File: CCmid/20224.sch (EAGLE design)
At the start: 17 parts, among them J3 9296006, K1 PC357NJ0000F, U1 AL8862

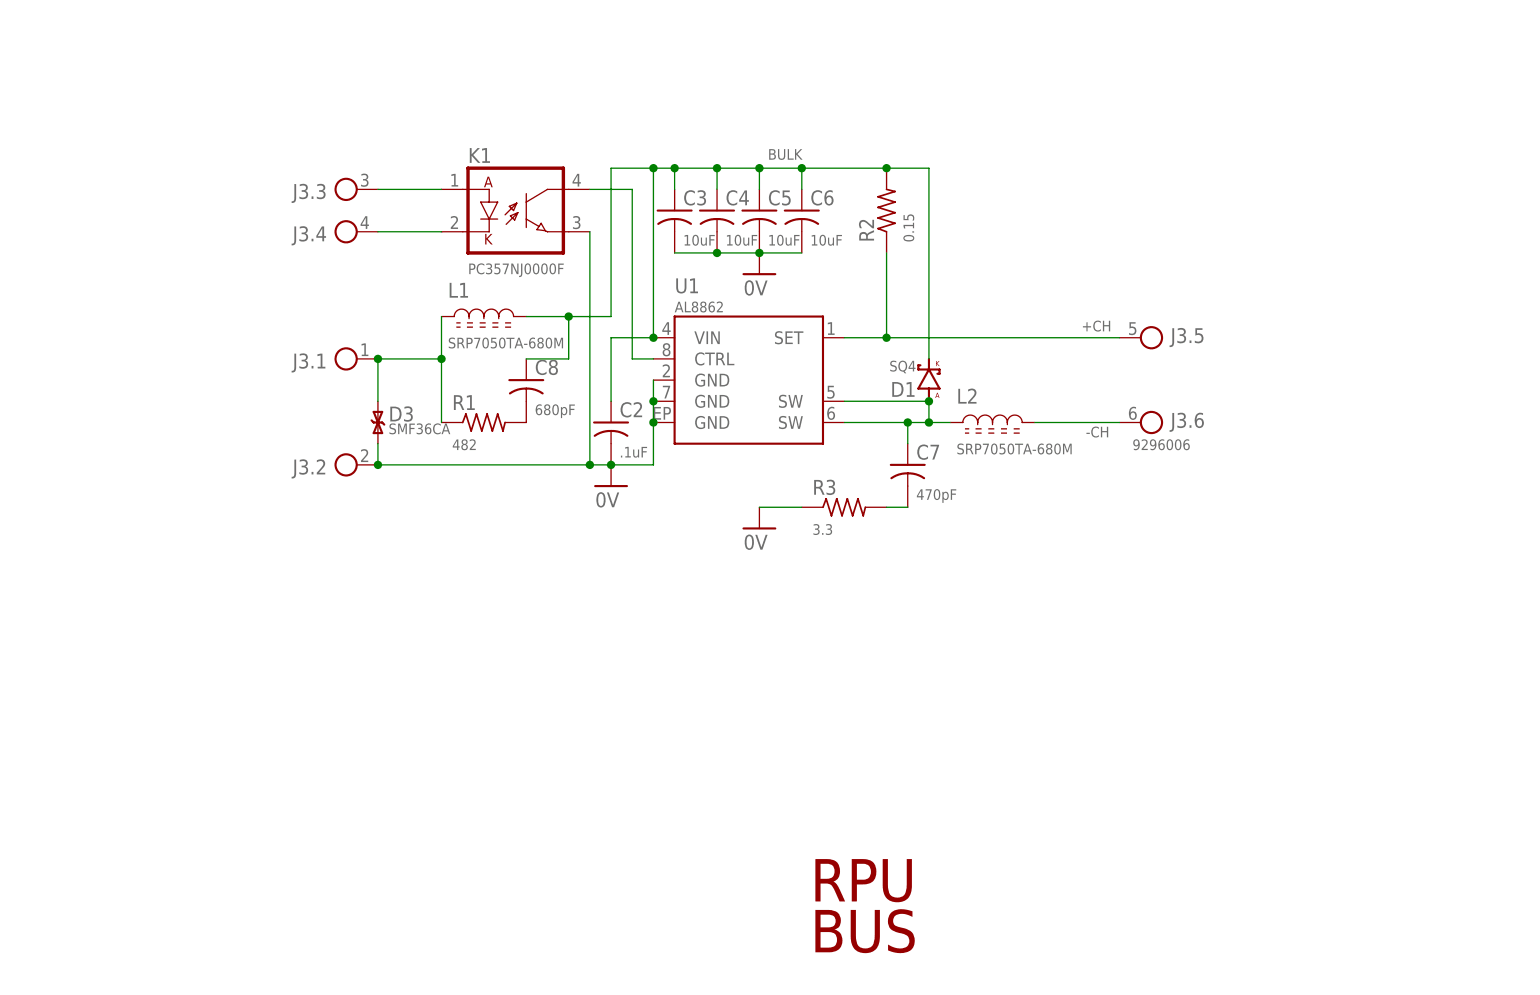
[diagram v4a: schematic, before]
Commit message: CCmid: fix inrush on schm
inrush 3A6 with 36V step
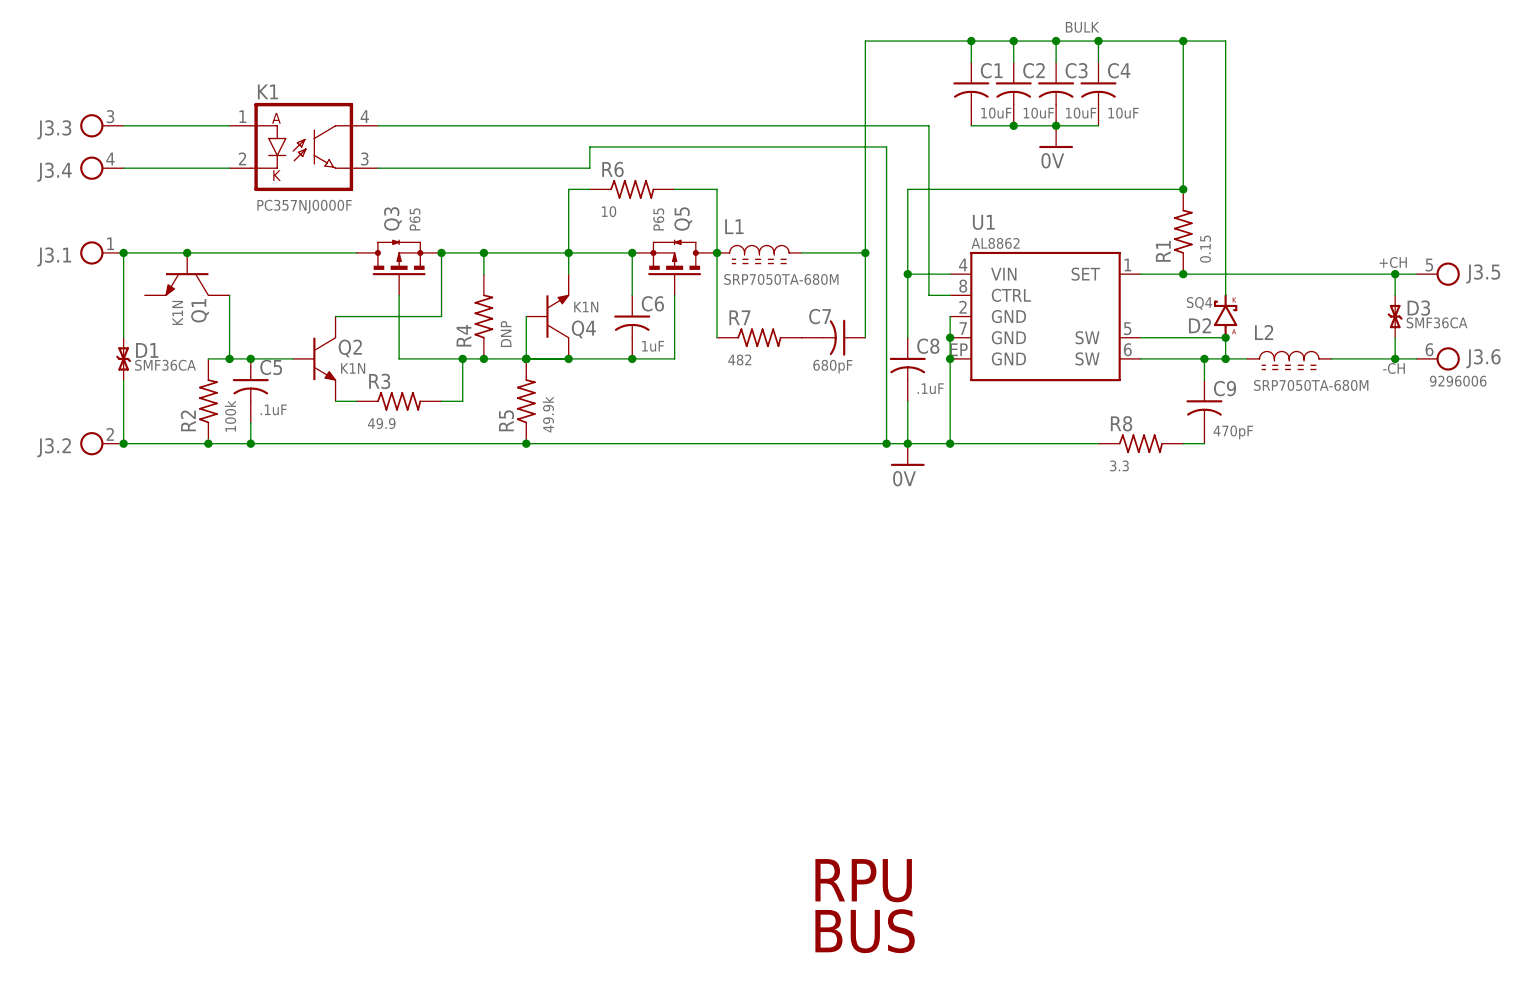
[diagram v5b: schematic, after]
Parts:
- added C1: 10uF, C-C:CC1206
- added C9: 470pF, C-C:CC0603A
- added D2: SQ4, D-SBR:DSMA
- added Q1, Q2, Q4: K1N, Q-NPN:NPNSOT23
- added Q3, Q5: P65, Q-PCH:N-CHSOT23
- added R4: DNP, R-C:R0805
- added R5: 49.9k, R-C:R0805
- added R6: 10, R-C:R1206
- added R7: 482, R-C:R0805
- added R8: 3.3, R-C:R0805
- C2: value .1uF -> 10uF; device C-C:CC0805A -> C-C:CC1206
- C5: value 10uF -> .1uF; device C-C:CC1206 -> C-C:CC0805A
- C6: value 10uF -> 1uF; device C-C:CC1206 -> C-C:CC0805A
- C7: value 470pF -> 680pF
- C8: value 680pF -> .1uF; device C-C:CC0603A -> C-C:CC0805A
- D1: value SQ4 -> SMF36CA; device D-SBR:DSMA -> D-TVS:TVS-BISOD123
- R1: value 482 -> 0.15; device R-C:R0805 -> R-C:R1210
- R2: value 0.15 -> 100k; device R-C:R1210 -> R-C:R0805
- R3: value 3.3 -> 49.9
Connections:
- new net N$10: Q2.E, R3.1
- new net N$32: C6.1, Q2.C, Q3.S, Q4.E, Q5.S, R4.2, R6.1
- new net N$33: C6.2, Q3.G, Q4.B, Q4.C, Q5.G, R3.2, R4.1, R5.2
- new net N$8: D1.C, J3.1.1, Q1.B, Q3.D
- new net N$9: C5.1, Q1.C, Q2.B, R2.2
- net +CH: now also D3.C, R1.1; no longer R2.1
- net -CH: now also D3.A
- net 0V: now also C1.2, C8.2, D1.A, R2.1, R5.1, R8.1; no longer C6.2, D3.A, R3.1
- net BULK: now also C1.1, C7.1, D2.K, R1.2; no longer C5.1, C6.1, D1.K, R2.2
- net N$3: now also C9.1, D2.A; no longer C7.1, D1.A
- net N$5: now also Q5.D, R6.2, R7.1; no longer D3.C, J3.1.1, R1.1
- net N$6: now also C9.2, R8.2; no longer C7.2, R3.2
- net N$7: now also C7.2, R7.2; no longer C8.2, R1.2
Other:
- note added: "Inrush bypass durring delay"
- note added: "L1 note: A self-resonance notch can hold onto energy and couple it to free space (377 Ohm), so it is better to impedance match and burn off as much as possible. The notch impedance is 482 Ohm."
- note added: "Soft inrush delay"
- note added: "Soft inrush reset"
- note removed: "30A inrush @36V on VIN."
- note removed: "A 58V peak lags inrush @36V on VIN."
- note removed: "A self-resonance notch can hold onto energy and couple it to free space (377 Ohm), so it is better to impedance match and burn off as much as possible. The notch impedance is 482 Ohm."
- moved on the sheet: C2, C3, C4, C5, C6, C7, C8, D3, J3.1, J3.2, J3.3, J3.4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

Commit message: CCmid: bom, surge sim
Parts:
- removed R8: 3.3, R-C:R0805
- added TP1: TPPAD1-06, J-TP:TPPAD1-06
- R1: value 0.15 -> 100k; device R-C:R1210 -> R-C:R0805
- R2: value 100k -> 49.9
- R3: value 49.9 -> 49.9k
- R4: value DNP -> 10; device R-C:R0805 -> R-C:R1206
- R5: value 49.9k -> 499
- R6: value 10 -> 3.3; device R-C:R1206 -> R-C:R0805
- R7: value 482 -> 0.15; device R-C:R0805 -> R-C:R1210
- renumbered J3 to J1
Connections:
- net +CH: now also R7.1; no longer R1.1
- net 0V: now also R1.1, R3.1, R6.1; no longer R2.1, R5.1, R8.1
- net BULK: now also R7.2; no longer R1.2
- net N$10: now also R2.1; no longer R3.1
- net N$3: now also TP1.TP
- net N$32: now also R4.1; no longer R4.2, R6.1
- net N$33: now also R2.2; no longer R4.1, R5.2
- net N$5: now also R4.2, R5.1; no longer R6.2, R7.1
- net N$6: now also R6.2; no longer R8.2
- net N$7: now also R5.2; no longer R7.2
- net N$9: now also R1.2; no longer R2.2
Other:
- note added: "12/19/21"
- note added: "AL8862, OPT, SOFT, SNUB FILTR+NOTCH SNUB"
- note added: "^1"
- moved on the sheet: R1, R2, R3, R4, R5, R6, R7
